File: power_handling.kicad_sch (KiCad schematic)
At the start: 57 parts, among them J2 usb_c, SW1 SMXS_01K_TP, U1 TPS62130, U12 FSUSB42MUX, U13 AP22802AW5-7, U2 MIC5365-1.8YC5-TR, U3 TPS62130, U4 TPS7A0309PDBVR

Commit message: complete redesign
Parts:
- removed C75: 100nF, Capacitor_SMD:C_0402_1005Metric, symbol Device:C
- removed C76: 100nF, Capacitor_SMD:C_0603_1608Metric, symbol Device:C
- removed D9: PESD0402V05, Diode_SMD:D_0402_1005Metric, symbol Diode:SZESD9B5.0ST5G
- removed R14: 10k, Resistor_SMD:R_0402_1005Metric, symbol Device:R
- removed R18, R19: 22R, Resistor_SMD:R_0402_1005Metric, symbol Device:R
- removed SW1: SMXS_01K_TP, Onju:SW-SMD_2P-L6.2-W2.5-LS9.4, symbol Switch:SW_DIP_x01
- removed U12: FSUSB42MUX, Package_SO:MSOP-10_3x3mm_P0.5mm, symbol Interface_USB:FSUSB42MUX
- renumbered C61 to C10, C63 to C11, C62 to C12, C6 to C13, C9 to C14, C64 to C15, C7 to C16, C10 to C17, C65 to C18, C8 to C19, C12 to C20, C66 to C21, C78 to C4, C77 to C5, C4 to C6, C5 to C7, C11 to C8, C79 to C9, D10 to D1, D11 to D2, D12 to D3, FB7 to FB1, J2 to J1, L3 to L1, L1 to L2, POWER_IN2 to POWER_IN1, R20 to R1, R76 to R10, R108 to R11, R77 to R12, R44 to R13, R46 to R14, R47 to R15, R1 to R2, R2 to R3, R21 to R4, R3 to R5, R22 to R6, U3 to U1, U13 to U2, U1 to U3, U2 to U4, U4 to U5
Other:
- note removed: "USB Data Switch"
- title: Nest mini drop in PCB replacement -> Drop in replacement PCB for Nest mini GEN2

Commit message: work in progress
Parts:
- added TP5, TP6, TP7, TP8: TestPoint, TestPoint:TestPoint_Pad_D1.0mm, symbol Connector:TestPoint
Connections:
- net +0V9: now also TP8.1
- net +1V8: now also TP7.1
- net +3V3: now also TP6.1
- net +5V: now also TP5.1

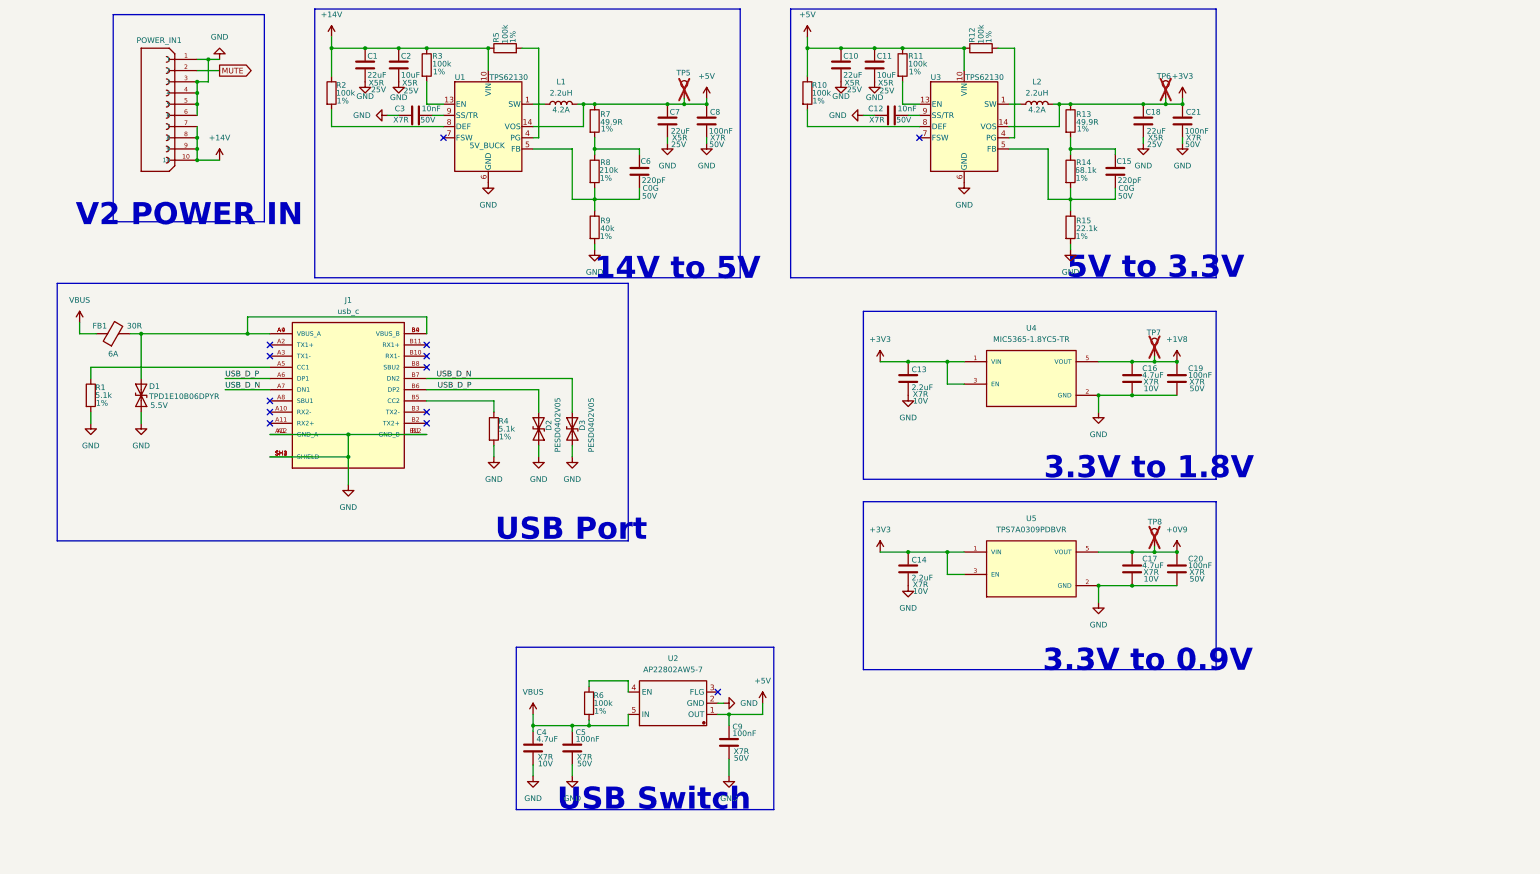
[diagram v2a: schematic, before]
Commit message: v2 hardware revision
MPR121 touch controller added to replace the esp32-s3 internal touch interface
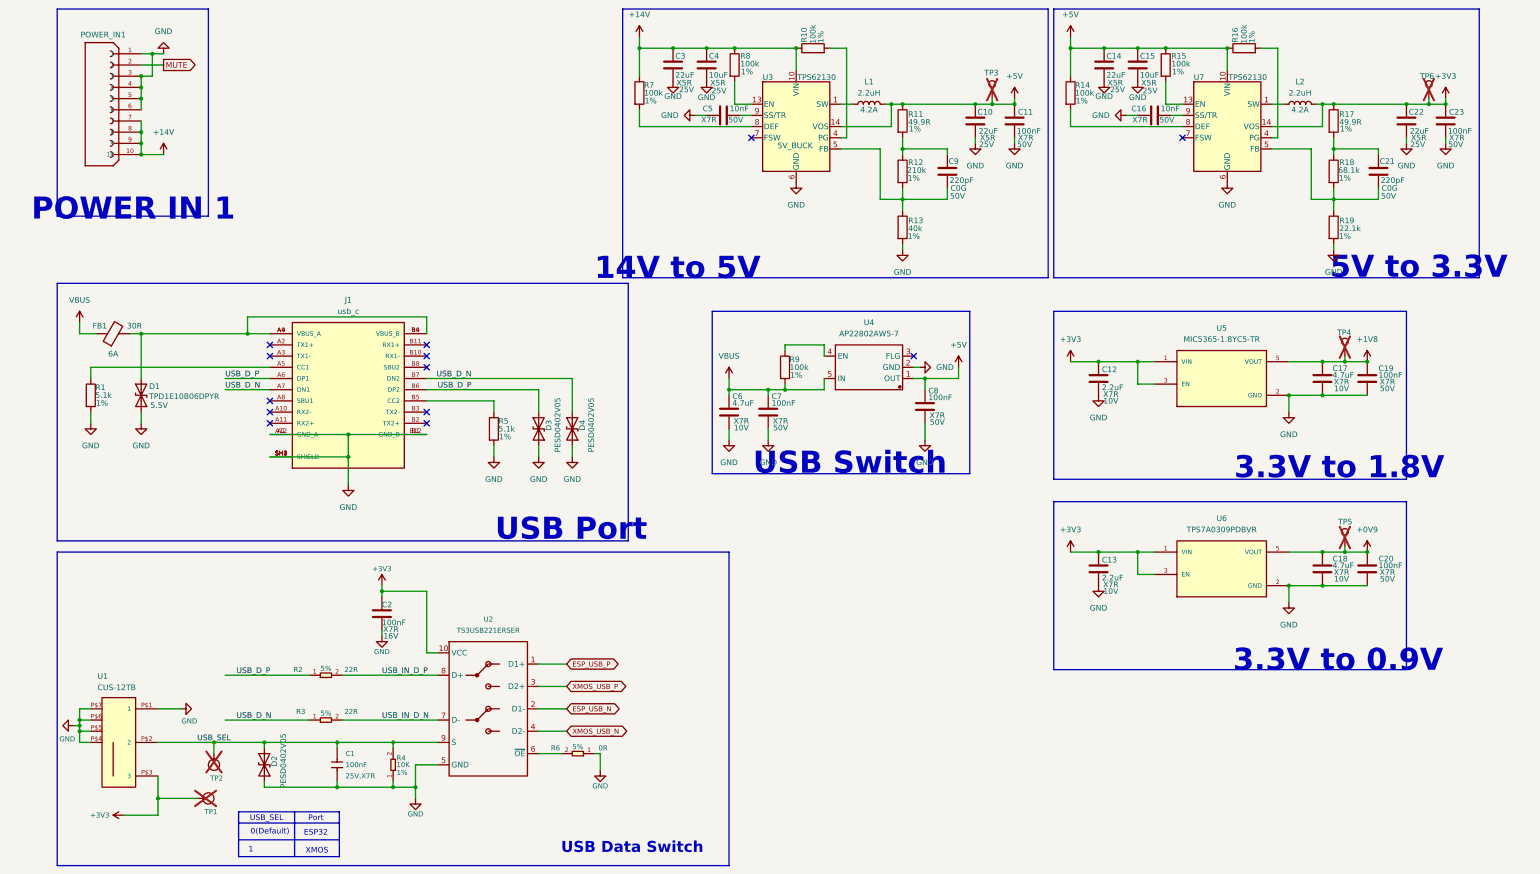
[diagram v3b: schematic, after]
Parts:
- added C1: 100nF, Capacitor_SMD:C_0402_1005Metric, symbol Seeed_libadl:Capacitors/302010024
- added C2: 100nF, Capacitor_SMD:C_0402_1005Metric, symbol Device:C
- added D2: PESD0402V05, Diode_SMD:D_0402_1005Metric, symbol Diode:SZESD9B5.0ST5G
- added R2, R3: 22R, Resistor_SMD:R_0402_1005Metric, symbol Seeed_libadl:Resistors/301010002
- added R4: 10K, Resistor_SMD:R_0402_1005Metric, symbol Seeed_libadl:Resistors/301010047
- added R6: 0R, Resistor_SMD:R_0402_1005Metric, symbol Seeed_libadl:Resistors/301010000
- added TP1: Test Point, TestPoint:TestPoint_Pad_D1.0mm, symbol Seeed_libdb:Misc/TP120C_SMD
- added TP2: Test Point, TestPoint:TestPoint_Pad_D1.0mm, symbol libdb:Misc/TP45C_SMD
- added U1: CUS-12TB, Onju:CUS-12B, symbol New_Library:CUS-12TB
- added U2: TS3USB221ERSER, Onju:TS3USB221ERSER, symbol Seeed_libdb:Ic/310100627
- renumbered C7 to C10, C8 to C11, C13 to C12, C14 to C13, C10 to C14, C11 to C15, C12 to C16, C16 to C17, C17 to C18, C15 to C21, C18 to C22, C21 to C23, C1 to C3, C2 to C4, C3 to C5, C4 to C6, C5 to C7, C9 to C8, C6 to C9, D2 to D3, D3 to D4, R5 to R10, R7 to R11, R8 to R12, R9 to R13, R10 to R14, R11 to R15, R12 to R16, R13 to R17, R14 to R18, R15 to R19, R4 to R5, R2 to R7, R3 to R8, R6 to R9, TP5 to TP3, TP7 to TP4, TP8 to TP5, U1 to U3, U2 to U4, U4 to U5, U5 to U6, U3 to U7
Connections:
- net +3V3: now also C2.1, TP1.1 (T), U1.P$3 (3), U2.10 (VCC)
- net GND: now also C1.2, C2.2, D2.1 (A1), R4.1, R6.1, U1.P$1 (1), U1.P$4, U1.P$5, U1.P$6, U1.P$7, U2.5 (GND)
- net USB_D_N: now also R3.1
- net USB_D_P: now also R2.1
- new net: R6.2, U2.6 (~{OE})
- new net ESP_USB_N: U2.2 (D1-)
- new net ESP_USB_P: U2.1 (D1+)
- new net USB_IN_D_N: R3.2, U2.7 (D-)
- new net USB_IN_D_P: R2.2, U2.8 (D+)
- new net USB_SEL: C1.1, D2.2 (A2), R4.2, TP2.1 (T), U1.P$2 (2), U2.9 (S)
- new net XMOS_USB_N: U2.4 (D2-)
- new net XMOS_USB_P: U2.3 (D2+)
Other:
- note added: "0(Default)"
- note added: "1"
- note added: "ESP32"
- note added: "POWER IN 1"
- note added: "Port"
- note added: "USB Data Switch"
- note added: "USB_SEL"
- note added: "XMOS"
- note removed: "V2 POWER IN"
- moved on the sheet: C10, C11, C12, C13, C14, C15, C16, C17, C18, C19, C20, C21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
